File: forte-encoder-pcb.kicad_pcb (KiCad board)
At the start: 2 copper layers, 36.5 x 45 mm, 59 parts, among them CN3(OUT)1 XT30(2+2)PB-M.G.B, J0 BM07B-SRSS-TB(LF)(SN), J1 Conn_01x01_Pin, J10 Conn_01x01_Pin, J2 Conn_01x01_Pin, J3 Conn_01x01_Pin, J4 Conn_01x01_Pin, J5 Conn_01x01_Pin, J6 Conn_01x01_Pin, J7 Conn_01x01_Pin, J8 Conn_01x01_Pin, J9 Conn_01x01_Pin, U2 STM32F103C8Tx, U3 MCP2542FD-E/MF, U4 MA732GQ-Z, U5 TPS629203DRLR, U6 TPS629203DRLR, Y1 CSTNE8M00G550000R0

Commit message: updated
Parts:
- moved TP12 20.8 mm to (100.0, 109.5)
- moved TP13 20.0 mm to (102.0, 108.8)
- moved TP14 16.4 mm to (99.3, 111.5)
- moved J3 13.5 mm to (103.5, 94.8)
- moved C28 13.1 mm to (115.1, 104.7)
- moved C29 13.1 mm to (115.1, 108.2)
- moved TP11 12.9 mm to (104.1, 101.5)
- moved C54 9.22 mm to (109.5, 96.5), turned to -90 degrees
- moved Y1 8.62 mm to (110.2, 99.5), turned to 180 degrees
- moved C33 8.60 mm to (107.0, 95.5), turned to 0 degrees
- moved U4 7.73 mm to (105.9, 98.7), turned to 0 degrees
- moved J5 6.51 mm to (114.0, 100.9)
- moved FL1 5.70 mm to (112.0, 97.5), turned to 180 degrees
- moved C24 5.51 mm to (112.0, 96.0), turned to 0 degrees
- moved R8 5.03 mm to (113.8, 110.5)
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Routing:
- net GND: track 25.1 -> 1.99 mm, vias 41 -> 69
- net /SCK: track 4.40 -> 19.8 mm, vias 0 -> 2
- net /CAN_RX: track 21.9 -> 9.75 mm, vias 2 -> 0
- net /CAN_TX: track 23.1 -> 11.6 mm
- net +3.3V: track 91.7 -> 80.7 mm, vias 12 -> 4
- net /MOSI: track 18.5 -> 8.24 mm, vias 2 -> 0
- net /CS: track 17.6 -> 12.6 mm, vias 0 -> 1
- net +5V: track 58.8 -> 63.2 mm, vias 1 -> 4
- net /USART_TX: track 28.1 -> 23.7 mm
- net /TMS: track 24.2 -> 28.4 mm
- net Net-(U2-VDDA): track 12.8 -> 8.73 mm, vias 4 -> 0
- net /NRST: track 28.4 -> 25.0 mm
- net /INDICATOR: track 1.97 -> 5.16 mm, vias 0 -> 2
- net /USART_RX: track 25.9 -> 22.9 mm
- net /TCK: track 26.8 -> 29.8 mm
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
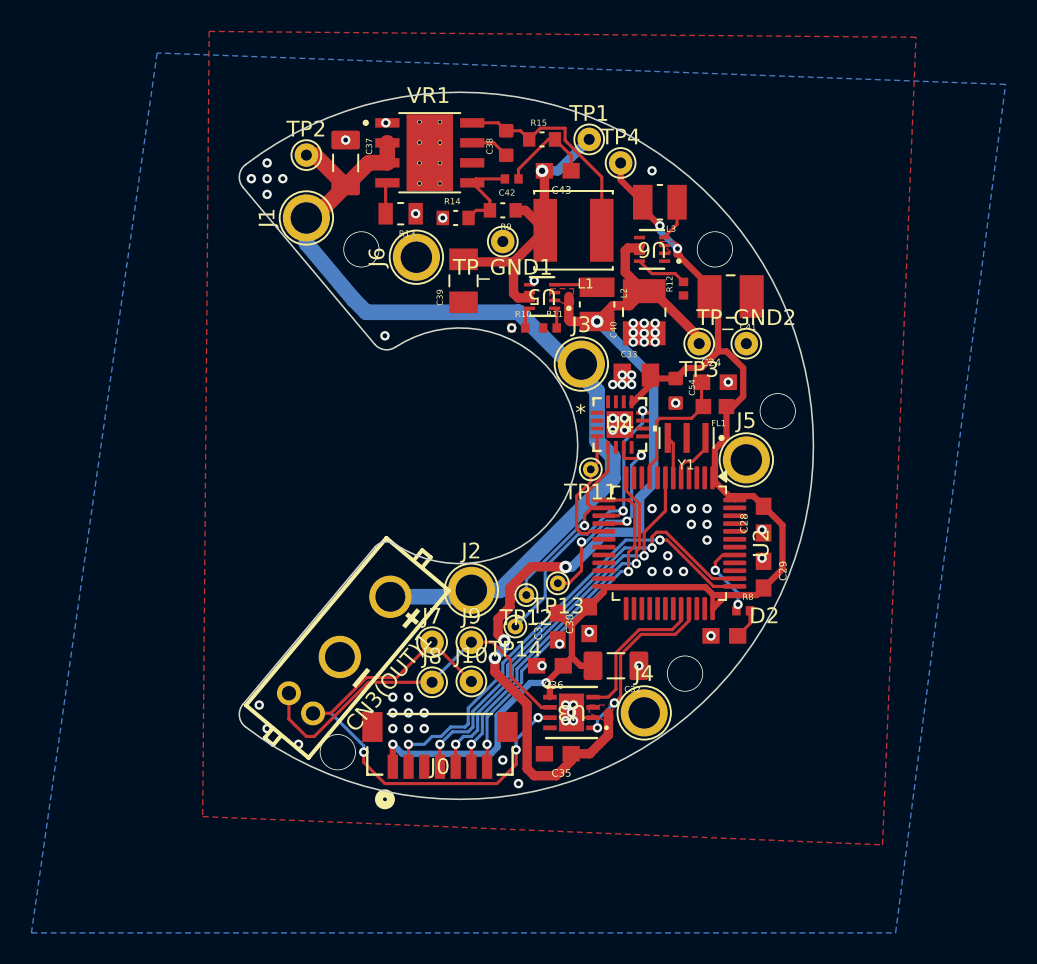
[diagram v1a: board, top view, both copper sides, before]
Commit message: rearange pcb
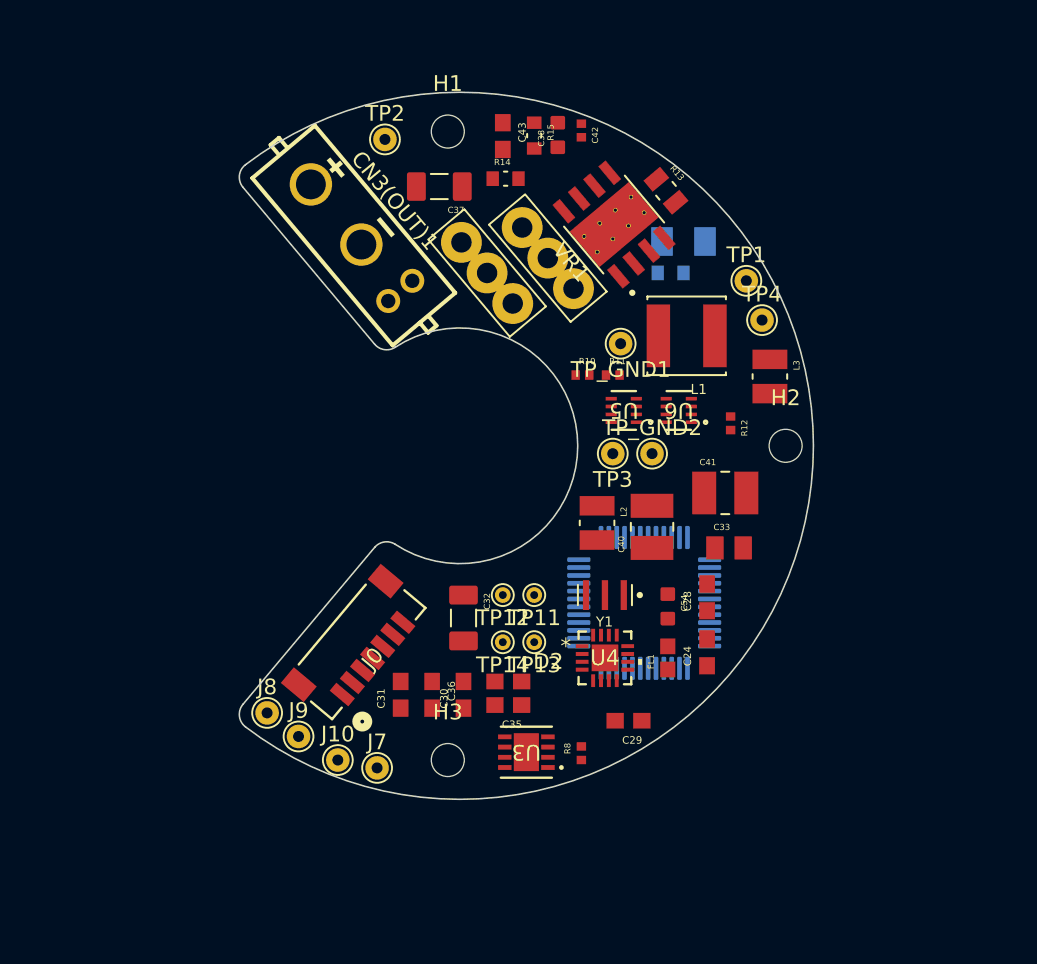
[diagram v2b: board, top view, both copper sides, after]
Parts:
- removed J2, J3, J5, J6: Conn_01x01_Pin, TestPoint:TestPoint_Plated_Hole_D2.0mm
- added H1: MountingHole, MountingHole:MountingHole_2.1mm, F.Cu at (95.0, 80.0)
- added H2: MountingHole, MountingHole:MountingHole_2.1mm, F.Cu at (116.5, 100.0)
- added H3: MountingHole, MountingHole:MountingHole_2.1mm, F.Cu at (95.0, 120.0)
- C39, R9, U2: moved to B.Cu
- J1, J4: footprint TestPoint:TestPoint_Plated_Hole_D2.0mm -> dash:solder_pad
- moved J4 29.7 mm to (97.5, 89.0), turned to 130 degrees
- moved CN3(OUT)1 26.3 mm to (89.1, 86.8), turned to -50 degrees
- moved C24 17.2 mm to (111.5, 113.2), turned to 90 degrees
- moved R13 16.9 mm to (108.9, 83.8), turned to -50 degrees
- moved FL1 16.3 mm to (109.0, 113.5), turned to 90 degrees
- moved J1 15.6 mm to (101.4, 88.1), turned to 130 degrees
- moved U4 14.9 mm to (105.0, 113.5)
- moved C39 14.2 mm to (110.0, 87.0), turned to 0 degrees
- moved D2 14.1 mm to (98.8, 115.0)
- moved L2 13.9 mm to (104.5, 104.9)
- moved C54 13.7 mm to (109.0, 110.2)
- moved R8 13.7 mm to (103.5, 119.6), turned to 90 degrees
- moved C40 13.7 mm to (108.0, 105.2)
- moved TP1 13.5 mm to (114.0, 89.5)
- moved TP4 13.5 mm to (115.0, 92.0)
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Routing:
- net +3.3V: track 80.7 -> 0.00 mm, vias 4 -> 0
- net +5V: track 63.2 -> 0.00 mm, vias 4 -> 0
- net +48V: track 58.6 -> 0.00 mm
- net /CAN+: track 33.2 -> 0.00 mm, vias 3 -> 0
- net /TCK: track 29.8 -> 0.00 mm, vias 2 -> 0
- net /TMS: track 28.4 -> 0.00 mm, vias 2 -> 0
- net /NRST: track 25.0 -> 0.00 mm, vias 2 -> 0
- net /USART_TX: track 23.7 -> 0.00 mm, vias 2 -> 0
- net /CAN-: track 23.6 -> 0.00 mm
- net /USART_RX: track 22.9 -> 0.00 mm, vias 2 -> 0
- net /SCK: track 19.8 -> 0.00 mm, vias 2 -> 0
- net +12V: track 19.4 -> 0.00 mm, vias 1 -> 0
- net /MISO: track 15.0 -> 0.00 mm, vias 3 -> 0
- net Net-(VR1-SW): track 14.1 -> 0.00 mm
- net /CS: track 12.6 -> 0.00 mm, vias 1 -> 0
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- removed copper zone on F.Cu, net +3.3V
- removed copper zone on F.Cu, net +5V
- removed copper zone on B.Cu, net GND
- removed copper zone on F.Cu, net GND
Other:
- copper layers 2 -> 4

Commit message: routing
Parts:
- moved C42 6.09 mm to (97.5, 81.0)
- moved R13 5.23 mm to (109.0, 89.0), turned to 180 degrees
- moved C54 4.56 mm to (109.0, 114.8)
- moved R8 3.39 mm to (102.1, 116.5), turned to 180 degrees
- moved FL1 3.27 mm to (109.0, 110.2)
- moved R11 2.88 mm to (103.4, 93.5), turned to 180 degrees
- moved C38 2.06 mm to (104.0, 80.7), turned to -90 degrees
- moved C37 1.58 mm to (93.0, 83.0)
- moved R12 1.58 mm to (112.5, 100.1), turned to 90 degrees
- moved R15 1.56 mm to (102.0, 80.7), turned to 90 degrees
- moved R9 1.50 mm to (109.2, 90.5)
- moved C31 1.30 mm to (92.0, 117.2), turned to -90 degrees
- moved J4 1.14 mm to (96.9, 88.1)
- moved VR1 1.12 mm to (106.1, 84.9), turned to 40 degrees
- moved C43 1.01 mm to (99.5, 80.2)
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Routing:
- net GND: track 0.00 -> 160.9 mm, vias 0 -> 8
- net +3.3V: track 0.00 -> 92.7 mm, vias 0 -> 4
- net /CAN-: track 0.00 -> 64.7 mm, vias 0 -> 2
- net /CAN+: track 0.00 -> 59.8 mm, vias 0 -> 2
- net +12V: track 0.00 -> 37.4 mm, vias 0 -> 1
- net +5V: track 0.00 -> 36.2 mm, vias 0 -> 3
- net /CS: track 0.00 -> 30.6 mm, vias 0 -> 2
- net /USART_RX: track 0.00 -> 27.8 mm, vias 0 -> 1
- net /MISO: track 0.00 -> 27.4 mm, vias 0 -> 1
- net Net-(VR1-FB): track 0.00 -> 26.2 mm, vias 0 -> 2
- net /USART_TX: track 0.00 -> 25.7 mm, vias 0 -> 1
- net +48V: track 0.00 -> 24.1 mm, vias 0 -> 1
- net /NRST: track 0.00 -> 23.9 mm, vias 0 -> 1
- net Net-(VR1-SW): track 0.00 -> 23.1 mm, vias 0 -> 2
- net /MOSI: track 0.00 -> 22.9 mm, vias 0 -> 2
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
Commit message: again
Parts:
- removed TP1: +12V TestPoint, TestPoint:TestPoint_THTPad_D1.5mm_Drill0.7mm
- removed TP3: +5V TestPoint, TestPoint:TestPoint_THTPad_D1.5mm_Drill0.7mm
- removed TP4: +3.3V TestPoint, TestPoint:TestPoint_THTPad_D1.5mm_Drill0.7mm
- removed TP_GND2: GND TestPoint, TestPoint:TestPoint_THTPad_D1.5mm_Drill0.7mm
- U4: moved to B.Cu
- moved U4 13.5 mm to (106.0, 100.0), turned to 180 degrees
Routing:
- net +12V: track 37.4 -> 36.5 mm
- added copper zone on F.Cu, net +12V

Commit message: fix
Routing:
- net /SCK: track 17.2 -> 54.6 mm, vias 1 -> 2
- net /MOSI: track 22.9 -> 40.2 mm
- net /MISO: track 27.4 -> 41.9 mm, vias 1 -> 2
- net GND: track 160.9 -> 173.9 mm, vias 8 -> 9
- net /CS: track 30.6 -> 42.7 mm
- net +5V: track 36.2 -> 33.5 mm
- net +3.3V: track 92.7 -> 94.6 mm, vias 4 -> 5
- net Net-(U5-SW): track 9.10 -> 10.1 mm
- net /NRST: track 23.9 -> 23.0 mm
- net /USART_TX: track 25.7 -> 24.8 mm
- net +12V: track 36.5 -> 36.8 mm, vias 1 -> 2

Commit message: design rule
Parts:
- C28, C29, C31, C32, C37: moved to B.Cu
- moved C31 17.1 mm to (103.5, 104.5)
- moved C43 14.4 mm to (112.0, 87.3), turned to -50 degrees
- moved C37 13.9 mm to (103.3, 92.3), turned to 40 degrees
- moved C30 9.88 mm to (103.5, 109.5), turned to 90 degrees
- moved D2 7.24 mm to (105.8, 117.2)
- moved C35 5.80 mm to (94.7, 112.5), turned to -90 degrees
- moved Y1 4.45 mm to (104.7, 113.9)
- moved R14 3.54 mm to (100.0, 79.7), turned to 90 degrees
- moved C29 3.21 mm to (103.4, 116.6), turned to 90 degrees
- moved R8 3.05 mm to (105.0, 115.8), turned to 0 degrees
- moved C28 2.50 mm to (113.5, 111.2), turned to -90 degrees
- moved C42 2.07 mm to (97.9, 79.0)
- moved C32 2.06 mm to (95.9, 108.9), turned to 0 degrees
- moved J1 1.92 mm to (99.9, 86.9)
- moved U3 1.63 mm to (100.1, 117.9), turned to -90 degrees
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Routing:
- net GND: track 173.9 -> 64.4 mm, vias 9 -> 17
- net +48V: track 24.1 -> 5.34 mm, vias 1 -> 0
- net +12V: track 36.8 -> 19.9 mm, vias 2 -> 5
- net Net-(C42-Pad1): track 5.60 -> 19.4 mm, vias 0 -> 3
- net +3.3V: track 94.6 -> 84.8 mm
- net /CS: track 42.7 -> 35.0 mm
- net /MISO: track 41.9 -> 34.3 mm
- net /MOSI: track 40.2 -> 33.2 mm
- net /CAN_RX: track 9.29 -> 16.2 mm, vias 1 -> 2
- net /RCC_OSC_IN: track 4.10 -> 10.2 mm, vias 1 -> 2
- net Net-(VR1-FB): track 26.2 -> 30.6 mm, vias 2 -> 3
- net /SCK: track 54.6 -> 51.7 mm
- net Net-(U2-VDDA): track 14.8 -> 12.0 mm
- net /USART_RX: track 27.3 -> 30.0 mm, vias 1 -> 2
- net /CAN+: track 59.8 -> 61.7 mm
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- added copper zone on B.Cu, net +12V
- added copper zone on B.Cu, net +48V
- added copper zone on F.Cu, net +48V
- added copper zone on In1.Cu, net +48V
- added copper zone on In2.Cu, net +48V
- added copper zone on In3.Cu, net +48V
- added copper zone on F.Cu, net +5V
- added copper zone on B.Cu, net GND
- added copper zone on F.Cu, net GND
- added copper zone on In1.Cu, net GND
- added copper zone on In2.Cu, net GND
- added copper zone on In3.Cu, net GND
- added copper zone on In4.Cu, net GND
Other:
- copper layers 4 -> 6

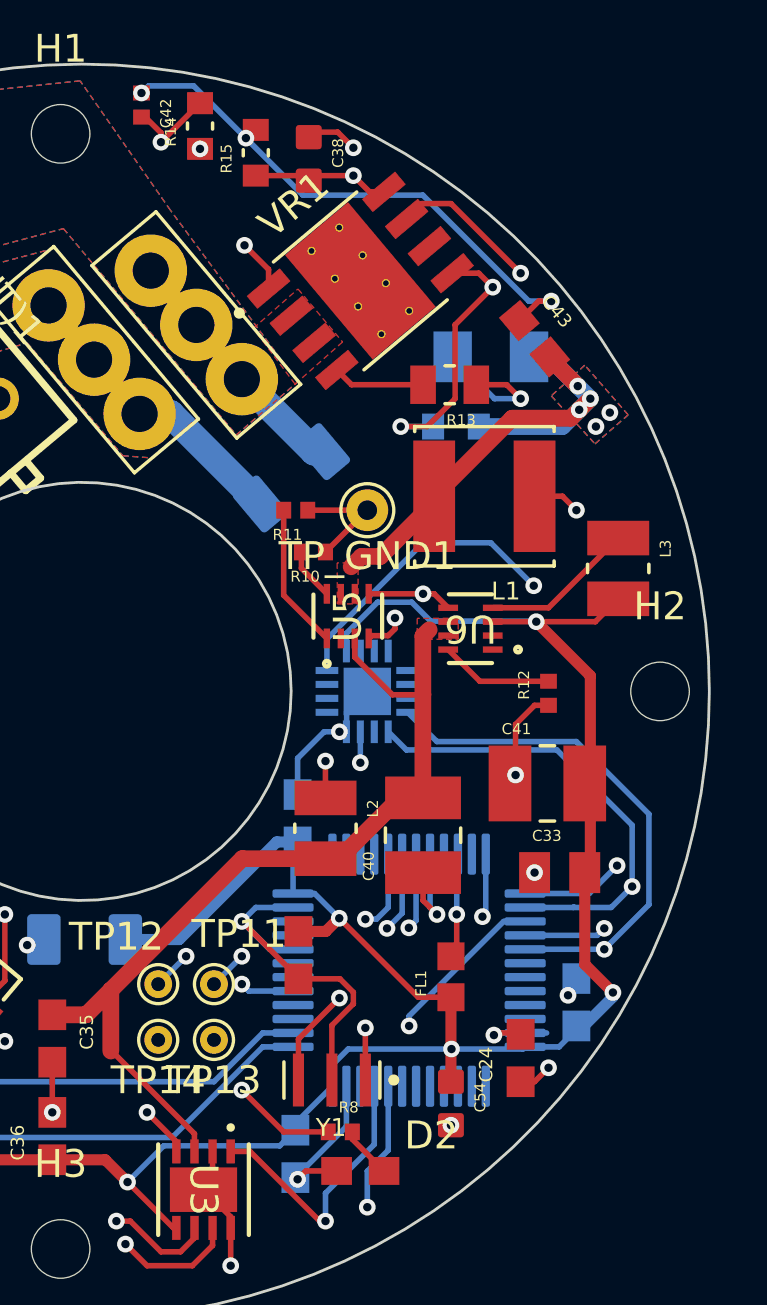
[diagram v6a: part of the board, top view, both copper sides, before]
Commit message: encoder capacitor
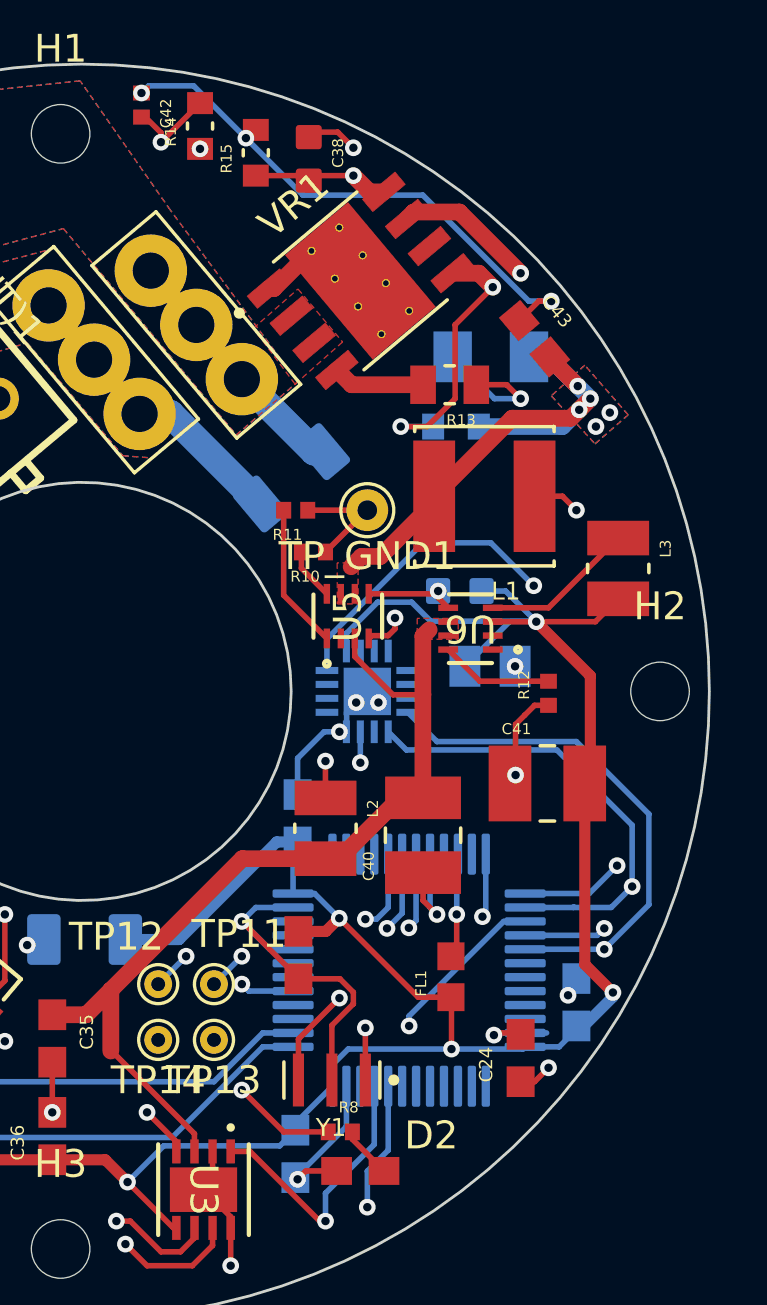
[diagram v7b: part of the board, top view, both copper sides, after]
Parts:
- C33, C54: moved to B.Cu
- moved C54 18.4 mm to (109.3, 96.4), turned to 180 degrees
- moved C33 7.81 mm to (110.4, 99.1), turned to 180 degrees
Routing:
- net +3.3V: track 84.8 -> 88.9 mm

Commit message: silkscreen
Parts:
- +    -: renamed from CN3(OUT)1
- TP GND: renamed from TP_GND1
- moved C35 1.60 mm to (96.3, 112.5)
- moved C36 1.60 mm to (96.3, 116.0)
- renumbered J8 to -, J7 to CAN+, J10 to CAN+, J9 to CAN-, TP12 to CS, TP13 to MISO, TP11 to MOSI, TP14 to SCK, TP2 to TP48V
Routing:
- net +5V: track 33.4 -> 31.3 mm
- net GND: track 64.8 -> 64.0 mm
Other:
- board text added: "+"
- board text added: "-"
- board text added: "3.3V"
- board text added: "48V"
- board text added: "GND"
- board text added: "NRST"
- board text added: "RX"
- board text added: "TCK"
- board text added: "TMS"
- board text added: "TX"
